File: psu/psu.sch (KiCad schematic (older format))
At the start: 57 parts

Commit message: Annotate
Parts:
- removed D? (x2): GRN, agg:0603-LED, symbol agg:LED
- removed R? (x2): 1k, agg:0603, symbol agg:R
- gave numbers to parts that had none: 53
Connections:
- net LED_OK1 is gone; now on net LED_FAULT: IC102.27 (PB4)
- net LED_FAULT: no longer IC102.30 (PB7)
- net LED_OK2: no longer names the net of IC102.28 (PB5)
- no-connect marks 12 -> 14

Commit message: Start PCB
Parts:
- added D112, D113, D114: ESD_DIODE, agg:0603, symbol agg:ESD_DIODE
- added J104: UART, agg:SM04B-PASS, symbol agg:CONN_01x04
- added R112, R113: 1k, agg:0603, symbol agg:R
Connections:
- net 3v3: now also D114.1, J104.1
- net GND: now also D112.2, D113.2, D114.2, J104.4
- net UART_TX: now also R113.2
- net UART_RX: now reaches IC102.30 (PB7)
- net UART_RX: now also R112.2
- new net: D113.1, J104.2, R113.1
- new net: D112.1, J104.3, R112.1
- no-connect marks 14 -> 13
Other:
- note added: "PB7: USART1_RX"
- moved on the sheet: D109, D110, D111, J102, R109, R110, R111

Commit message: More pcb layout
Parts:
- TP102: footprint agg:SIL-254P-01 -> agg:KEYSTONE5016
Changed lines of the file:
@@
 F 0 "TP102" H 2250 2150 50  0000 L CNN
 F 1 "TESTPAD" H 2250 2025 50  0001 L CNN
-F 2 "agg:SIL-254P-01" H 2250 1950 50  0001 L CNN
+F 2 "agg:KEYSTONE5016" H 2250 1950 50  0001 L CNN
 F 3 "" H 2250 2100 50  0001 C CNN
 	1    2250 2100

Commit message: routing
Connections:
- net VQ is gone; now on net V_Q: IC102.12 (PA6), IC102.14 (PB0)
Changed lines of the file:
@@
 	7450 1150 7350 1150
 Connection ~ 7350 1150
-$Comp
-L agg:CONN_01x03 J103
-U 1 1 5D637956
-P 10550 1000
-AR Path="/5D637956" Ref="J103"  Part="1"
-AR Path="/6147A5D5/5D637956" Ref="J?"  Part="1"
-F 0 "J103" H 10500 1100 50  0000 L CNN
-F 1 "HV_OUT" V 10450 900 50  0000 C CNN
-F 2 "agg:MOLEX-KK-254P-03" H 10550 1000 50  0001 C CNN
-F 3 "" H 10550 1000 50  0001 C CNN
-F 4 "1360131" H 10550 1000 50  0001 C CNN "Farnell"
-	1    10550 1000
-	-1   0    0    -1
-$EndComp
 $Sheet
 S 9050 900  650  1100
@@
 V_Q
 Text Label 5050 4950 0    50   ~ 0
-VQ
+V_Q
 Wire Wire Line
 	5050 4950 4950 4950
@@
 PB0: COMP4_IN+
 Text Label 5050 3850 0    50   ~ 0
-VQ
+V_Q
 Wire Wire Line
 	5050 3850 4950 3850
@@
 Wire Wire Line
 	10050 3900 10050 3950
+$Comp
+L agg:CONN_01x03 J103
+U 1 1 5D637956
+P 10550 1000
+AR Path="/5D637956" Ref="J103"  Part="1"
+AR Path="/6147A5D5/5D637956" Ref="J?"  Part="1"
+F 0 "J103" H 10500 1100 50  0000 L CNN
+F 1 "HV_OUT" V 10450 900 50  0000 C CNN
+F 2 "agg:MOLEX-KK-254P-03" H 10550 1000 50  0001 C CNN
+F 3 "" H 10550 1000 50  0001 C CNN
+F 4 "1360131" H 10550 1000 50  0001 C CNN "Farnell"
+	1    10550 1000
+	-1   0    0    -1
+$EndComp
 $EndSCHEMATC

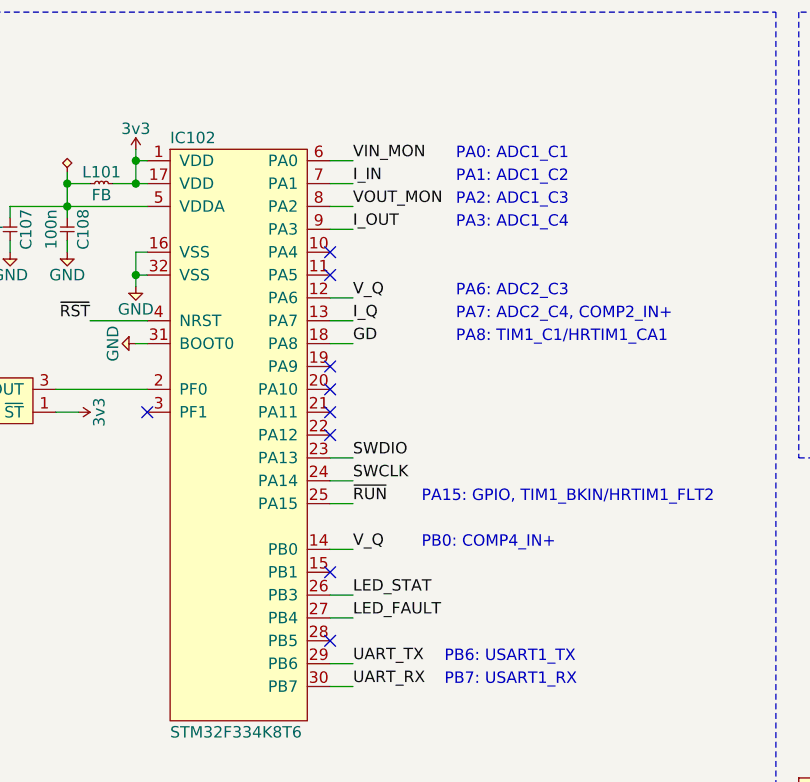
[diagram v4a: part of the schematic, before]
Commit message: Complete routing. But maybe the transformer is the wrong way around.
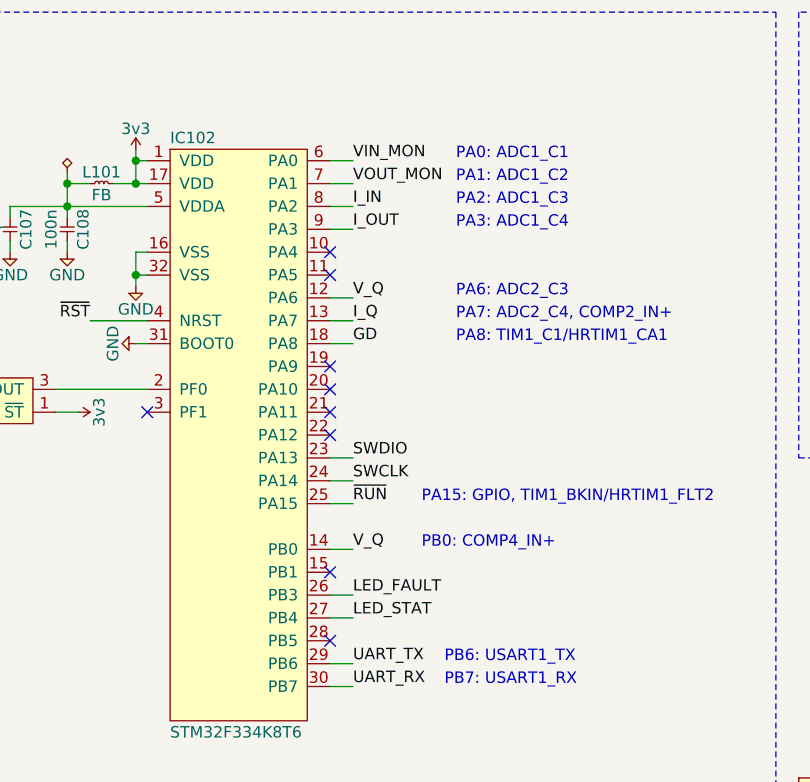
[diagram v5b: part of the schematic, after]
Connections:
- net I_IN: now also IC102.8 (PA2); no longer IC102.7 (PA1)
- net LED_FAULT: now also IC102.26 (PB3); no longer IC102.27 (PB4)
- net LED_STAT: now also IC102.27 (PB4); no longer IC102.26 (PB3)
- net VOUT_MON: now also IC102.7 (PA1); no longer IC102.8 (PA2)
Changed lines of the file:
@@
 Text Label 5050 3250 0    50   ~ 0
 VIN_MON
-Text Label 5050 3450 0    50   ~ 0
+Text Label 5050 3350 0    50   ~ 0
 VOUT_MON
 Wire Notes Line
@@
 Wire Wire Line
 	5550 6150 5650 6150
+Text Label 5050 5150 0    50   ~ 0
+LED_FAULT
 Text Label 5050 5250 0    50   ~ 0
-LED_FAULT
-Text Label 5050 5150 0    50   ~ 0
 LED_STAT
 $Comp
@@
 Text Label 8950 1000 2    50   ~ 0
 GD
-Text Label 5050 3350 0    50   ~ 0
+Text Label 5050 3450 0    50   ~ 0
 I_IN
 Text Notes 3200 2450 0    60   ~ 12

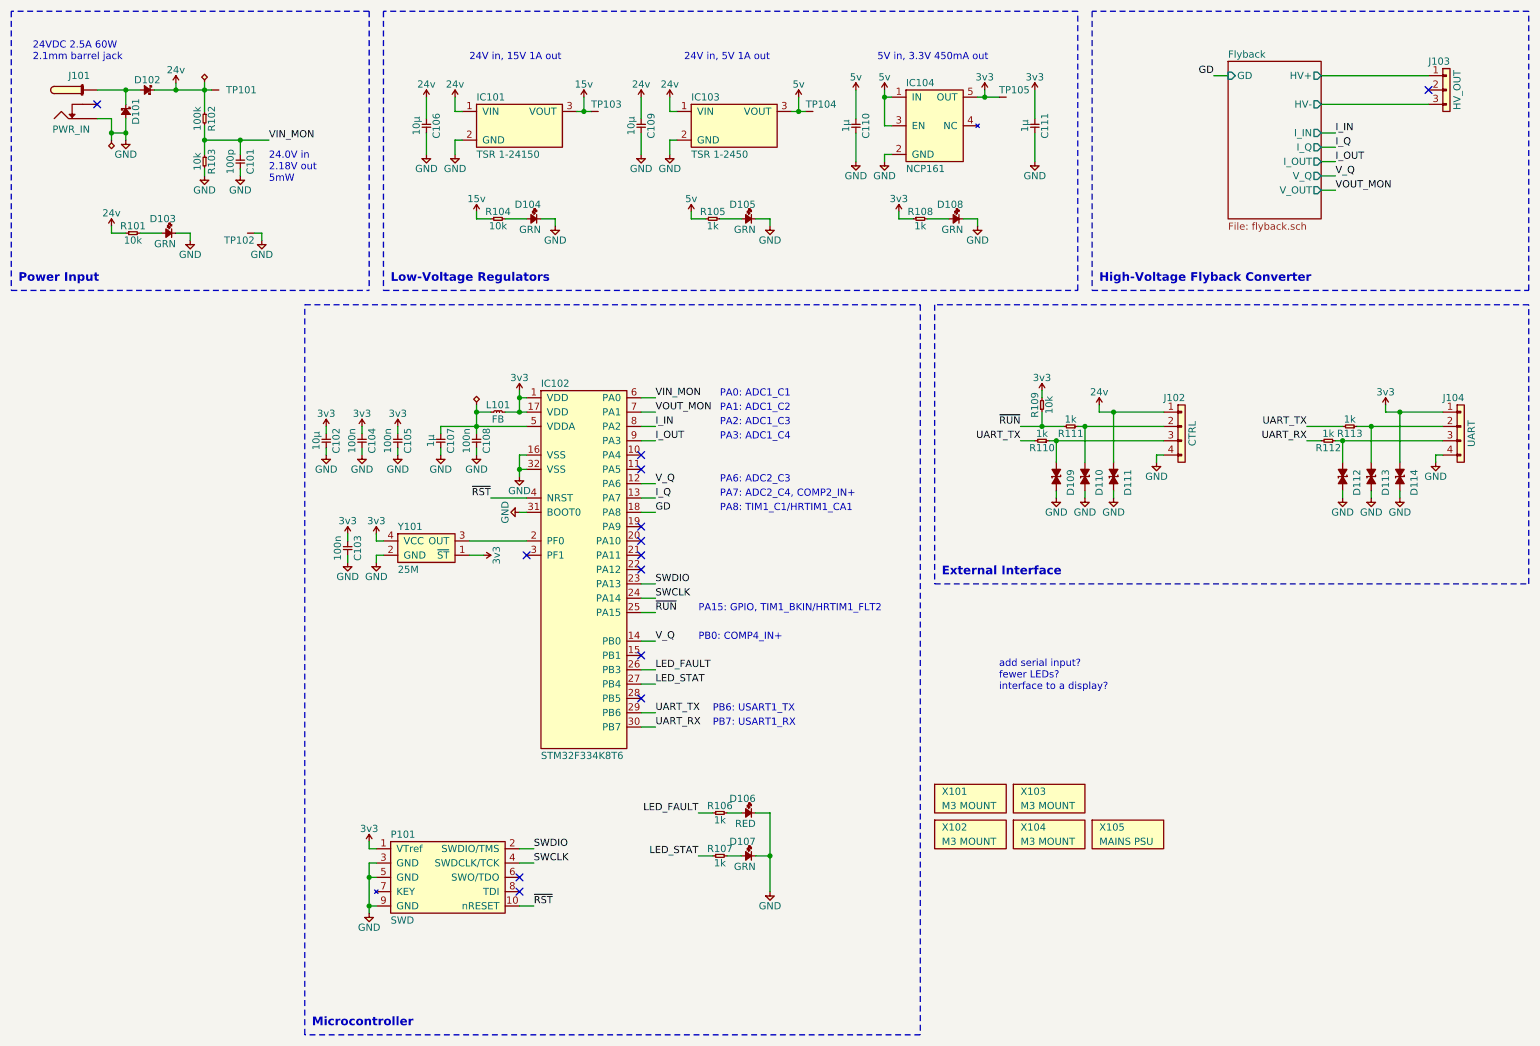
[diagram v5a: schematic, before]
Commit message: Complete routing take 2, with transformer secondary pins swapped
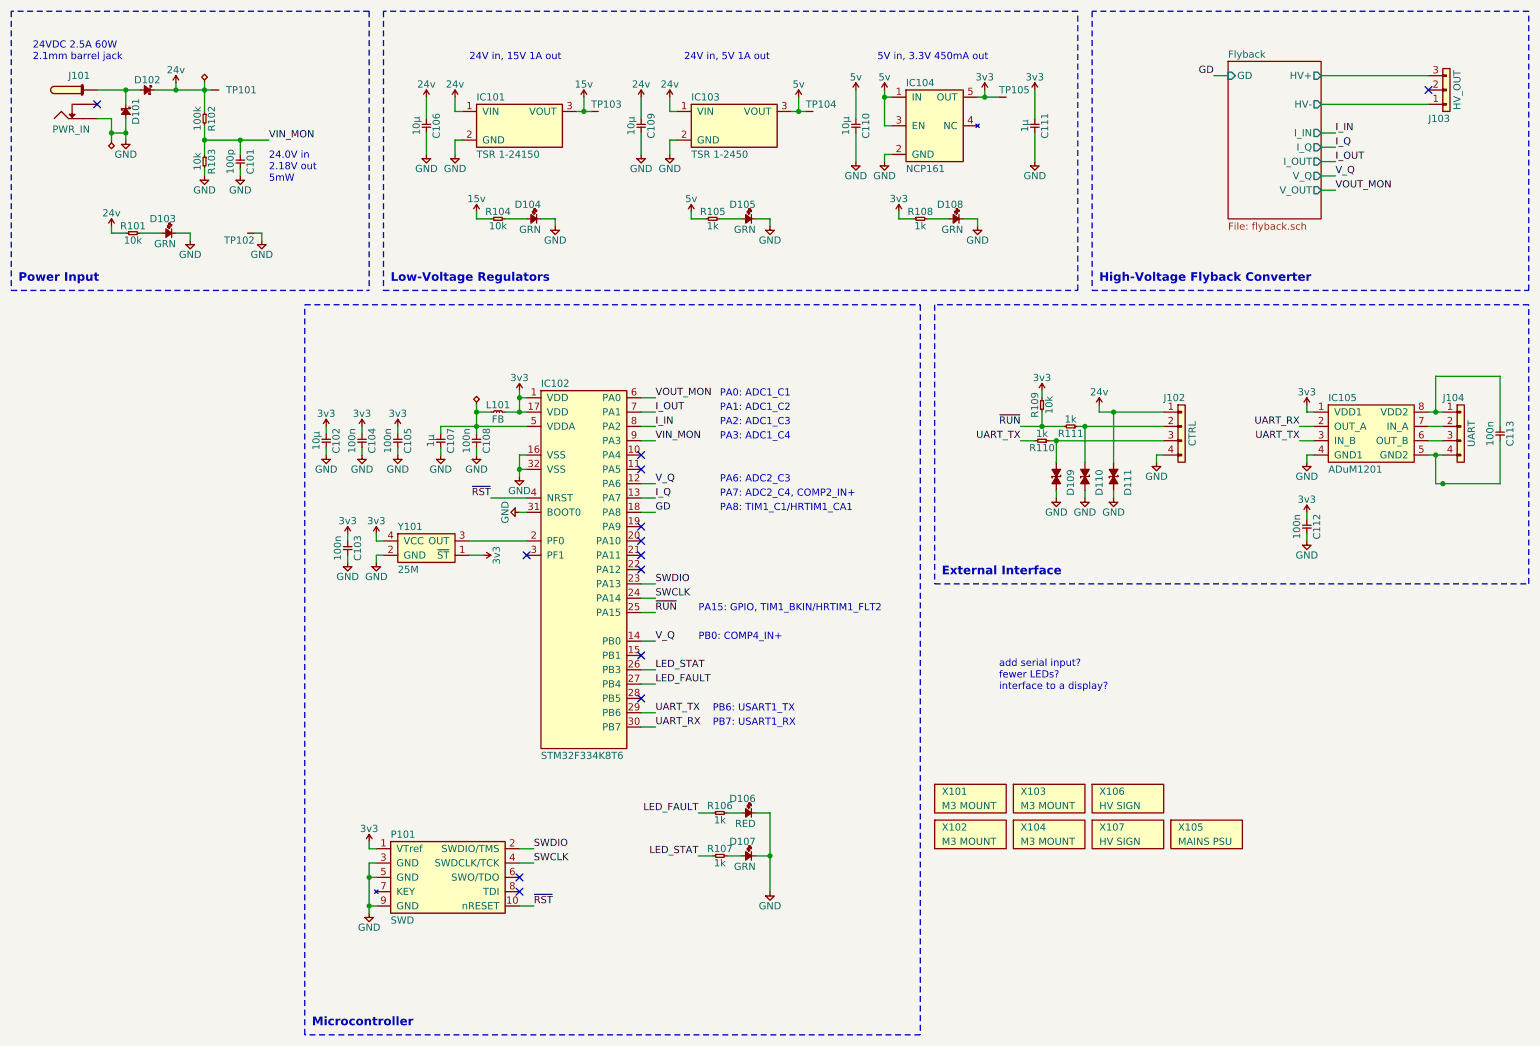
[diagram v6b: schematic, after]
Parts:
- removed D112, D113, D114: ESD_DIODE, agg:0603, symbol agg:ESD_DIODE
- removed R112, R113: 1k, agg:0603, symbol agg:R
- added C112, C113: 100n, agg:0603, symbol agg:C
- added IC105: ADuM1201, agg:SOIC-8, symbol agg:ADuM1201
- added X106, X107: HV SIGN, psu:hv, symbol agg:PART
- C110: value 1µ -> 10µ; footprint agg:0603 -> agg:1210; Farnell 2320814 -> 2781426; Voltage 16V -> 50V
- J104: footprint agg:SM04B-PASS -> agg:MOLEX-PICOBLADE-53398-0471; Farnell 2399347 -> 1125367
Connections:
- net 3v3: now also C112.1, IC105.1 (VDD1); no longer J104.1
- net Flyback/HV+: now also J103.3; no longer J103.1
- net Flyback/HV-: now also J103.1; no longer J103.3
- net GND: now also C112.2, IC105.4 (GND1); no longer J104.4
- net I_OUT: now also IC102.7 (PA1); no longer IC102.9 (PA3)
- net LED_FAULT: now also IC102.27 (PB4); no longer IC102.26 (PB3)
- net LED_STAT: now also IC102.26 (PB3); no longer IC102.27 (PB4)
- net UART_RX: now also IC105.2 (OUT_A)
- net UART_TX: now also IC105.3 (IN_B)
- net VIN_MON: now also IC102.9 (PA3); no longer IC102.6 (PA0)
- net VOUT_MON: now also IC102.6 (PA0); no longer IC102.7 (PA1)
- net at J104.2: now also IC105.7 (IN_A)
- net at J104.3: now also IC105.6 (OUT_B)
- new net: C113.1, IC105.8 (VDD2), J104.1
- new net: C113.2, IC105.5 (GND2), J104.4
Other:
- moved on the sheet: X105

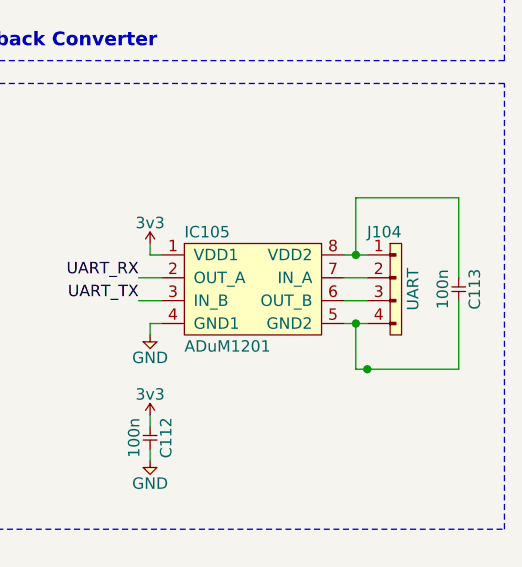
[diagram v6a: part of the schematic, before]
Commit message: Tidy up tracks. RFM r1.
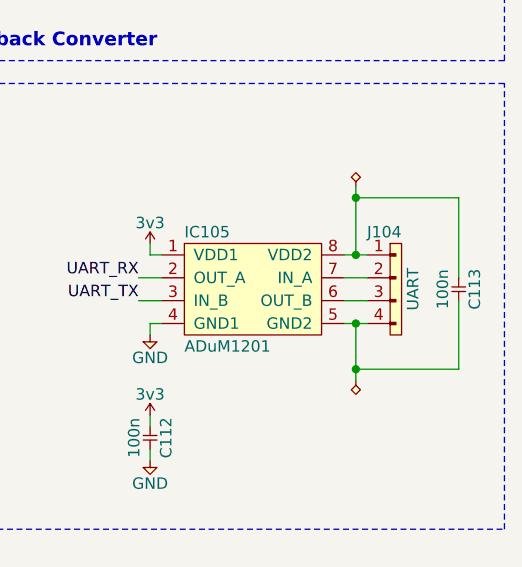
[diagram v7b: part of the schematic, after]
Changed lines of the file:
@@
 	10500 3650 10500 3850
-Wire Wire Line
-	10500 3850 10550 3850
 Wire Wire Line
 	10950 3850 10950 3550
@@
 	1    0    0    -1
 $EndComp
-Connection ~ 10550 3850
+$Comp
+L agg:PWR #FLG?
+U 1 1 604AC01E
+P 10500 3050
+F 0 "#FLG?" H 10500 3210 50  0001 C CNN
+F 1 "PWR" H 10500 3140 50  0001 C CNN
+F 2 "" H 10500 3050 50  0001 C CNN
+F 3 "" H 10500 3050 50  0001 C CNN
+	1    10500 3050
+	1    0    0    -1
+$EndComp
 Wire Wire Line
-	10550 3850 10950 3850
+	10500 3050 10500 3100
+Wire Wire Line
+	10500 3850 10950 3850
+Connection ~ 10500 3100
+$Comp
+L agg:PWR #FLG?
+U 1 1 604B67BA
+P 10500 3900
+F 0 "#FLG?" H 10500 4060 50  0001 C CNN
+F 1 "PWR" H 10500 3990 50  0001 C CNN
+F 2 "" H 10500 3900 50  0001 C CNN
+F 3 "" H 10500 3900 50  0001 C CNN
+	1    10500 3900
+	-1   0    0    1
+$EndComp
+Wire Wire Line
+	10500 3900 10500 3850
+Connection ~ 10500 3850
 $EndSCHEMATC

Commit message: Update Farnell part numbers
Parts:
- TP102: Farnell (none) -> 2292858
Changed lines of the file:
@@
 F 2 "agg:KEYSTONE5016" H 2250 1950 50  0001 L CNN
 F 3 "" H 2250 2100 50  0001 C CNN
+F 4 "2292858" H 2250 2100 50  0001 C CNN "Farnell"
 	1    2250 2100
 	-1   0    0    1
@@
 $EndComp
 $Comp
-L agg:PWR #FLG?
+L agg:PWR #FLG0106
 U 1 1 604AC01E
 P 10500 3050
-F 0 "#FLG?" H 10500 3210 50  0001 C CNN
+F 0 "#FLG0106" H 10500 3210 50  0001 C CNN
 F 1 "PWR" H 10500 3140 50  0001 C CNN
 F 2 "" H 10500 3050 50  0001 C CNN
@@
 Connection ~ 10500 3100
 $Comp
-L agg:PWR #FLG?
+L agg:PWR #FLG0107
 U 1 1 604B67BA
 P 10500 3900
-F 0 "#FLG?" H 10500 4060 50  0001 C CNN
+F 0 "#FLG0107" H 10500 4060 50  0001 C CNN
 F 1 "PWR" H 10500 3990 50  0001 C CNN
 F 2 "" H 10500 3900 50  0001 C CNN
